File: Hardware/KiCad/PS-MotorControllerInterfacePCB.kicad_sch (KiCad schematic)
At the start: 45 parts, among them J1 53307-2471, J3 PWR + CAN, J4 PEAK, J5 Power MPPT

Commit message: revB
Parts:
- removed J3: PWR + CAN, Connector_Molex:Molex_Nano-Fit_105309-xx06_1x06_P2.50mm_Vertical, symbol Connector_Generic:Conn_01x06
- removed J4: PEAK, Connector_Molex:Molex_Nano-Fit_105309-xx02_1x02_P2.50mm_Vertical, symbol Connector_Generic:Conn_01x02
- removed J5: Power MPPT, UTSVT_Connectors:Molex_Nano-Fit_105309-xx02_1x02_P2.50mm_Vertical, symbol Connector_Generic:Conn_01x02
- removed Moco-in1: MotorController-in, UTSVT_Connectors:Molex_Microfit3.0_02x03_6-Pin-Vertical-PCB-Receptacle_447690601, symbol Connector_Generic:Conn_02x03_Top_Bottom
- removed Moco-out1: MotorController-out, UTSVT_Connectors:Molex_Microfit3.0_02x03_6-Pin-Vertical-PCB-Receptacle_447690601, symbol Connector_Generic:Conn_02x03_Top_Bottom
- removed Z1: SMAF4751A-TP, UTSVT_Passives:SODFL5026X125N, symbol UTSVT_Power:SMAF4749A-TP
- removed Z4: SMAF4744A, UTSVT_Passives:SODFL5026X125N, symbol UTSVT_Power:SMAF4749A-TP
- added 12V?: VIN_24V, TestPoint:TestPoint_Pad_1.0x1.0mm, symbol Connector:TestPoint
- added 12V?: 24V, TestPoint:TestPoint_Pad_1.0x1.0mm, symbol Connector:TestPoint
- added 12V?: 12V, TestPoint:TestPoint_Pad_1.0x1.0mm, symbol Connector:TestPoint
- added 12V?: 12V_BUS, TestPoint:TestPoint_Pad_1.0x1.0mm, symbol Connector:TestPoint
- added D1, D2: D_TVS, symbol Device:D_TVS
- added J2: can out of mppts and moco into board, symbol Connector_Generic:Conn_01x03
- added J3: PWR board, symbol Connector_Generic:Conn_01x02
- added J4: can into board, symbol Connector_Generic:Conn_02x03_Counter_Clockwise
- added J5: can out of board into mppts and moco, symbol Connector_Generic:Conn_01x03
- added J6: Candapter, symbol Connector_Generic:Conn_01x02
- added J8: PWR Moco, symbol Connector_Generic:Conn_01x02
- added J9: can out of board, symbol Connector_Generic:Conn_02x03_Counter_Clockwise
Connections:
- net +12V: now also 12V?.1, J8.1 (Pin_1)
- net +24V: now also 12V?.1, J3.1 (Pin_1)
- net 12V_BUS: now also 12V?.1, D2.2 (A2)
- net CAN_N: now also J2.2 (Pin_2), J4.2 (Pin_2), J5.2 (Pin_2), J6.2 (Pin_2), J9.2 (Pin_2)
- net CAN_P: now also J2.1 (Pin_1), J4.1 (Pin_1), J5.1 (Pin_1), J6.1 (Pin_1), J9.1 (Pin_1)
- net GND: now also D1.1 (A1), D2.1 (A1), J2.3 (Pin_3), J3.2 (Pin_2), J4.3 (Pin_3), J5.3 (Pin_3), J8.2 (Pin_2), J9.3 (Pin_3)
- net VIN_24V: now also 12V?.1, D1.2 (A2)
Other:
- note added: "stub before termination"
- note removed: "VCU -> moco-in -> moco-out -> interface terminate on VCU and interface"
- moved on the sheet: H1, H2, H4, J1, JP1, R11, R12, R17, R_A_TACH_PD1, R_B_TACH_PD1, TP1, TP3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

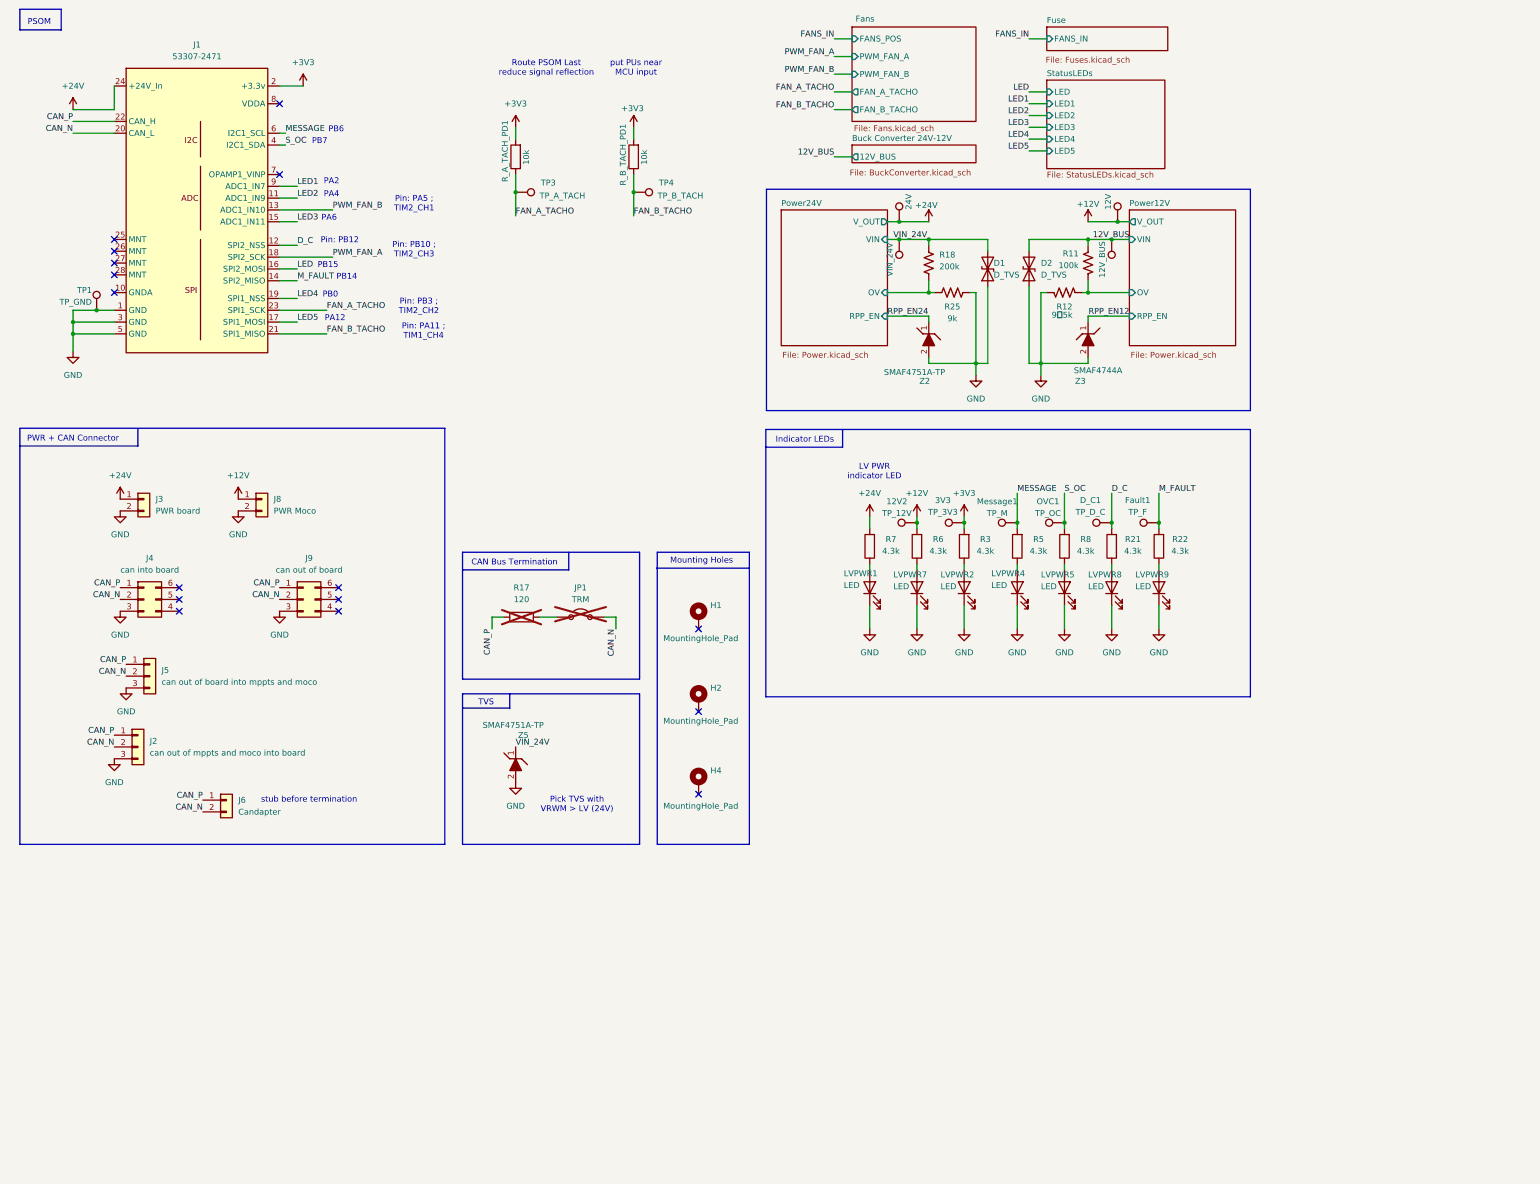
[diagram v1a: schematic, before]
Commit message: schematic changes, pre pcb revB changes
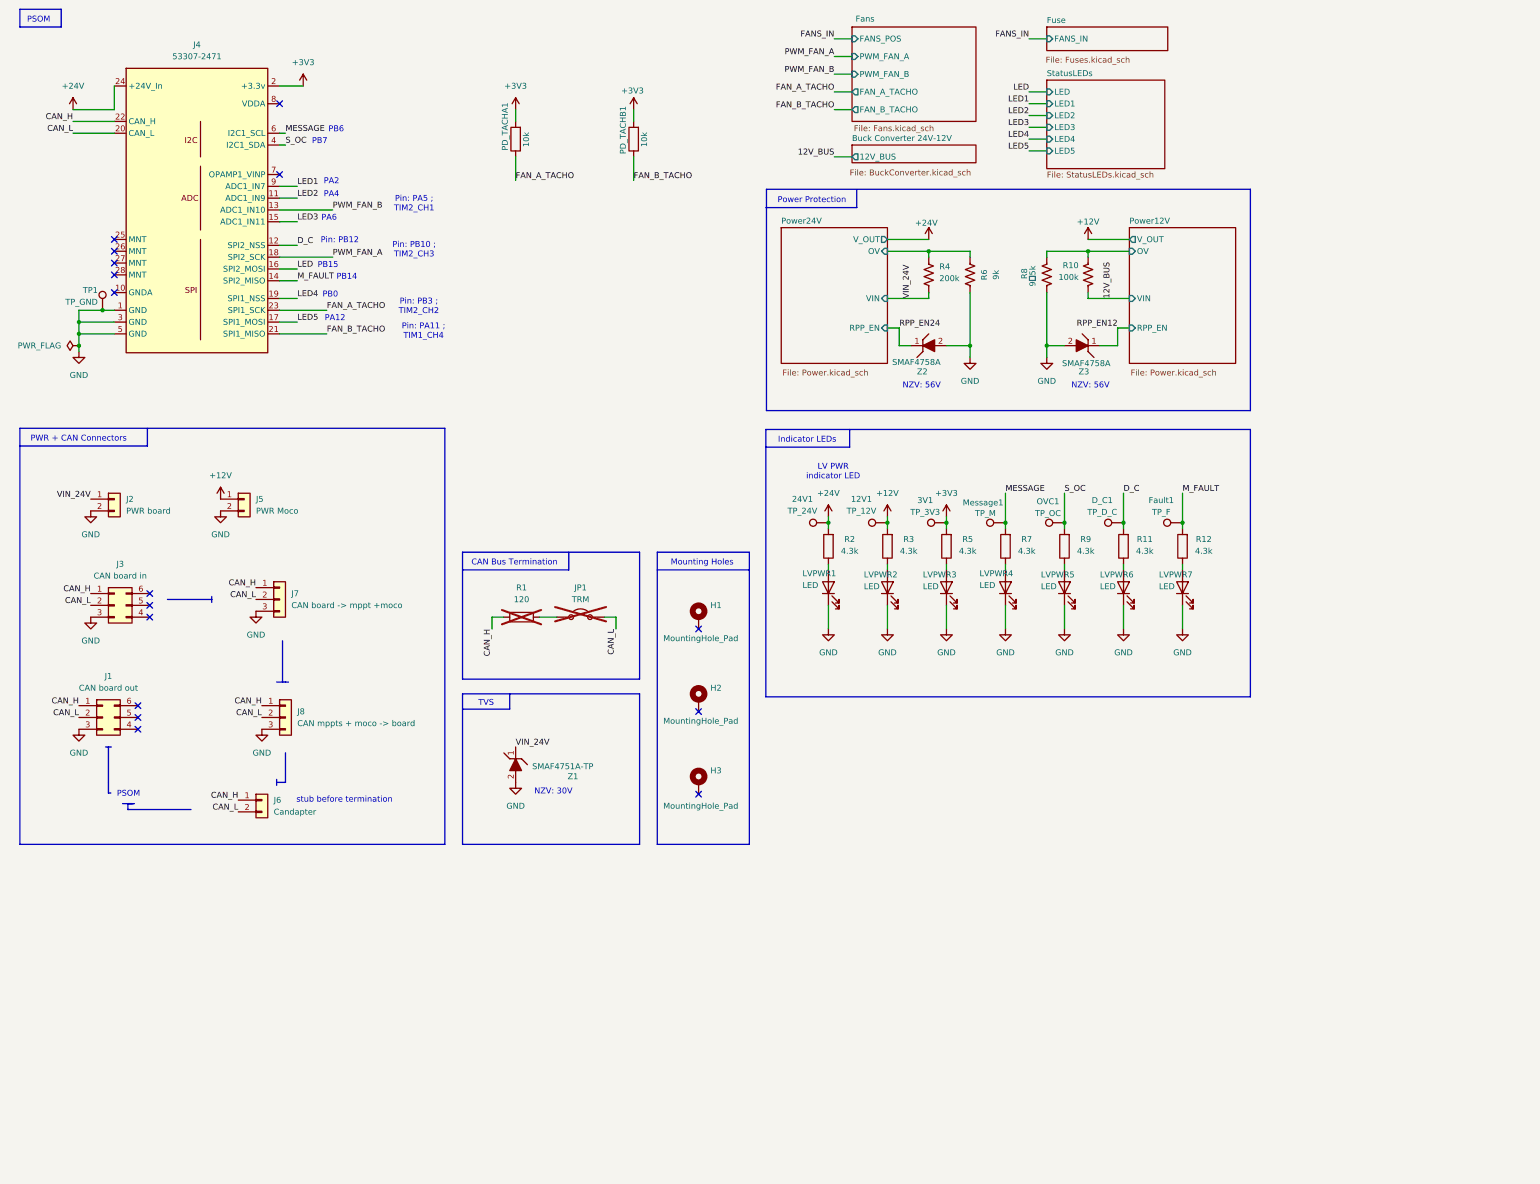
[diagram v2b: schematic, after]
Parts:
- removed 12V?: VIN_24V, TestPoint:TestPoint_Pad_1.0x1.0mm, symbol Connector:TestPoint
- removed 12V?: 24V, TestPoint:TestPoint_Pad_1.0x1.0mm, symbol Connector:TestPoint
- removed 12V?: 12V, TestPoint:TestPoint_Pad_1.0x1.0mm, symbol Connector:TestPoint
- removed 12V?: 12V_BUS, TestPoint:TestPoint_Pad_1.0x1.0mm, symbol Connector:TestPoint
- removed D1, D2: D_TVS, symbol Device:D_TVS
- removed TP3: TP_A_TACH, TestPoint:TestPoint_Pad_1.0x1.0mm, symbol Connector:TestPoint
- removed TP4: TP_B_TACH, TestPoint:TestPoint_Pad_1.0x1.0mm, symbol Connector:TestPoint
- added 24V1: TP_24V, TestPoint:TestPoint_Pad_1.0x1.0mm, symbol Connector:TestPoint
- J1: renamed from J9; value can out of board -> CAN board out; footprint (none) -> Connector_Molex:Molex_Nano-Fit_105314-xx06_2x03_P2.50mm_Horizontal
- J2: renamed from J3; footprint (none) -> Connector_Molex:Molex_Nano-Fit_105313-xx02_1x02_P2.50mm_Horizontal
- J3: renamed from J4; value can into board -> CAN board in; footprint (none) -> Connector_Molex:Molex_Nano-Fit_105314-xx06_2x03_P2.50mm_Horizontal
- J5: renamed from J8; footprint (none) -> Connector_Molex:Molex_Nano-Fit_105313-xx02_1x02_P2.50mm_Horizontal
- J6: footprint (none) -> Connector_Molex:Molex_Nano-Fit_105313-xx02_1x02_P2.50mm_Horizontal
- J7: renamed from J5; value can out of board into mppts and moco -> CAN board -> mppt +moco; footprint (none) -> Connector_Molex:Molex_Nano-Fit_105313-xx03_1x03_P2.50mm_Horizontal
- J8: renamed from J2; value can out of mppts and moco into board -> CAN mppts + moco -> board; footprint (none) -> Connector_Molex:Molex_Nano-Fit_105313-xx03_1x03_P2.50mm_Horizontal
- R1: renamed from R17; LCSC (none) -> C22787
- R10: renamed from R11; LCSC (none) -> C25803
- R11: renamed from R21; LCSC (none) -> C2907165
- R12: renamed from R22; LCSC (none) -> C2907165
- R2: renamed from R7; LCSC (none) -> C2907165
- R3: renamed from R6; LCSC (none) -> C2907165
- R4: renamed from R18; LCSC (none) -> C25811
- R5: renamed from R3; LCSC (none) -> C2907165
- R6: renamed from R25; LCSC (none) -> C166911
- R7: renamed from R5; LCSC (none) -> C2907165
- R9: renamed from R8; LCSC (none) -> C2907165
- Z1: renamed from Z5; LCSC (none) -> C5754725
- Z2: value SMAF4751A-TP -> SMAF4758A; LCSC (none) -> C183490; Mouser Part Number 833-SMAF4751A-TP -> (none)
- Z3: value SMAF4744A -> SMAF4758A; LCSC (none) -> C183490; Mouser Part Number 833-SMAF4744A-TP -> (none)
- renumbered 12V2 to 12V1, 3V3 to 3V1, H4 to H3, J1 to J4, LVPWR7 to LVPWR2, LVPWR2 to LVPWR3, LVPWR8 to LVPWR6, LVPWR9 to LVPWR7, R_A_TACH_PD1 to PD_TACHA1, R_B_TACH_PD1 to PD_TACHB1, R12 to R8
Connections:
- net +24V: now also 24V1.1; no longer J2.1 (Pin_1)
- net 12V_BUS: now also R10.2; no longer R10.1
- net GND: now also R6.1; no longer R6.2
- net Power12V/OV: now also R10.1; no longer R10.2
- net Power24V/OV: now also R4.1, R6.2; no longer R4.2, R6.1
- net VIN_24V: now also J2.1 (Pin_1), R4.2; no longer R4.1
- net CAN_N renamed CAN_L
- net CAN_P renamed CAN_H
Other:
- note added: "NZV: 30V"
- note added: "NZV: 56V"
- note added: "PWR + CAN Connectors"
- note added: "Power Protection"
- note removed: "PWR + CAN Connector"
- note removed: "Pick TVS with VRWM > LV (24V)"
- note removed: "Route PSOM Last reduce signal reflection"
- note removed: "put PUs near MCU input"
- moved on the sheet: 12V1, 3V1, D_C1, Fault1, J1, J2, J3, J5, J6, J7, J8, LVPWR1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

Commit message: sch changes, pre pcb changes
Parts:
- removed PD_TACHA1, PD_TACHB1: 10k, Resistor_SMD:R_0603_1608Metric_Pad0.98x0.95mm_HandSolder, symbol Device:R
- removed R10: 100k, Resistor_SMD:R_0603_1608Metric_Pad0.98x0.95mm_HandSolder, symbol Device:R_US
- removed R4: 200k, Resistor_SMD:R_0603_1608Metric_Pad0.98x0.95mm_HandSolder, symbol Device:R_US
- removed R6: 9k, Resistor_SMD:R_0603_1608Metric_Pad0.98x0.95mm_HandSolder, symbol Device:R_US
- removed R8: 9。5k, Resistor_SMD:R_0603_1608Metric_Pad0.98x0.95mm_HandSolder, symbol Device:R_US
- removed Z2, Z3: SMAF4758A, UTSVT_Passives:SODFL5026X125N, symbol UTSVT_Power:SMAF4749A-TP
- added LED6, LED7: LED, LED_SMD:LED_0603_1608Metric, symbol Device:LED
- added R7, R8: 4.3k, Resistor_SMD:R_0603_1608Metric_Pad0.98x0.95mm_HandSolder, symbol Device:R
- added TP_1: LED1, TestPoint:TestPoint_Pad_1.0x1.0mm, symbol Connector:TestPoint
- added TP_2: LED2, TestPoint:TestPoint_Pad_1.0x1.0mm, symbol Connector:TestPoint
- D_C1: value TP_D_C -> TP_DC
- H1, H2, H3: footprint MountingHole:MountingHole_3.2mm_M3 -> MountingHole:MountingHole_3.2mm_M3_Pad_TopBottom
- J1: renamed from J2; footprint Connector_Molex:Molex_Nano-Fit_105313-xx02_1x02_P2.50mm_Horizontal -> UTSVT_Connectors:105313-2102
- J2: renamed from J1; footprint Connector_Molex:Molex_Nano-Fit_105314-xx06_2x03_P2.50mm_Horizontal -> UTSVT_Connectors:105314-1306
- J3: footprint Connector_Molex:Molex_Nano-Fit_105314-xx06_2x03_P2.50mm_Horizontal -> UTSVT_Connectors:105314-1306
- J4: renamed from J6; footprint Connector_Molex:Molex_Nano-Fit_105313-xx02_1x02_P2.50mm_Horizontal -> UTSVT_Connectors:105313-2102
- J6: renamed from J7; footprint Connector_Molex:Molex_Nano-Fit_105313-xx03_1x03_P2.50mm_Horizontal -> UTSVT_Connectors:105313-1103
- J7: renamed from J8; footprint Connector_Molex:Molex_Nano-Fit_105313-xx03_1x03_P2.50mm_Horizontal -> UTSVT_Connectors:105313-1103
- J8: renamed from J5; footprint Connector_Molex:Molex_Nano-Fit_105313-xx02_1x02_P2.50mm_Horizontal -> UTSVT_Connectors:105313-2102
- renumbered J4 to J5, LVPWR3 to LED1, LVPWR4 to LED2, LVPWR5 to LED3, LVPWR6 to LED4, LVPWR7 to LED5, LVPWR2 to LED8, R5 to R1, R3 to R10, R7 to R2, R9 to R3, R1 to R4, R11 to R5, R12 to R6, R2 to R9
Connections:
- net LED4 is gone; now on net LED1: J5.19 (SPI1_NSS)
- net LED5 is gone; now on net LED2: J5.17 (SPI1_MOSI)
- net VIN_24V is gone; now on net +24V: J1.1 (Pin_1), Z1.1 (K)
- net +24V: no longer 24V1.1, R9.2
- net GND: now also LED6.1 (K), LED7.1 (K)
- net LED1: now also R7.2, TP_1.1; no longer J5.9 (ADC1_IN7)
- net LED2: now also R8.2, TP_2.1; no longer J5.11 (ADC1_IN9)
- net LED renamed LATCH
- net LED3 renamed ST
- new net: LED6.2 (A), R7.1
- new net: LED7.2 (A), R8.1
- new net 12V_SENSE: J5.9 (ADC1_IN7)
- new net Buck Converter 24V-12V/24VIN: 24V1.1, R9.2
- new net EN: J5.11 (ADC1_IN9)
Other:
- removed sheet Fuse
- removed sheet Power24V
- removed sheet StatusLEDs
- added sheet HSS (HSS.kicad_sch)
- sheet Buck Converter 24V-12V ports: added 12V_SENSE, 24VIN; removed none
- sheet Power12V ports: added VOUT; removed OV, RPP_EN, V_OUT
- note added: "CAN Connectors"
- note removed: "Indicator LEDs"
- note removed: "LV PWR indicator LED"
- note removed: "NZV: 56V"
- note removed: "PWR + CAN Connectors"
- note removed: "Power Protection"
- note removed: "TVS"
- moved on the sheet: 12V1, 24V1, 3V1, D_C1, Fault1, H1, H2, H3, J1, J2, J3, J4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

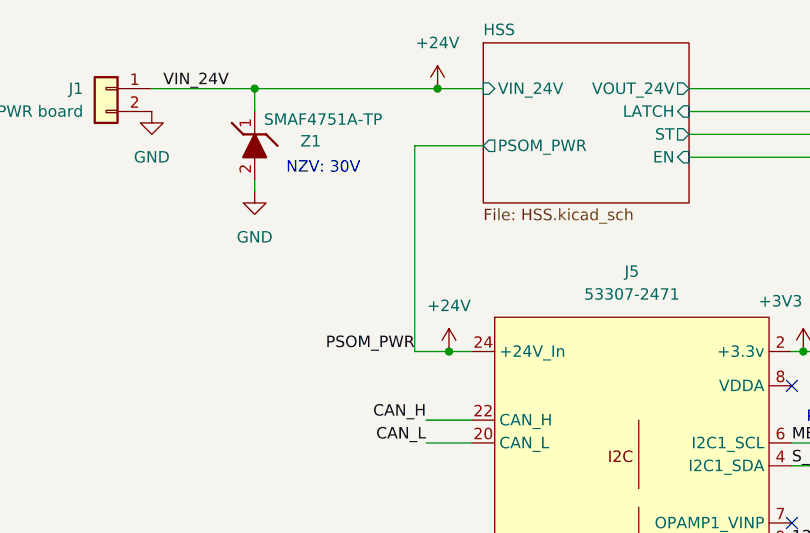
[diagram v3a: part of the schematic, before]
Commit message: fuse fix
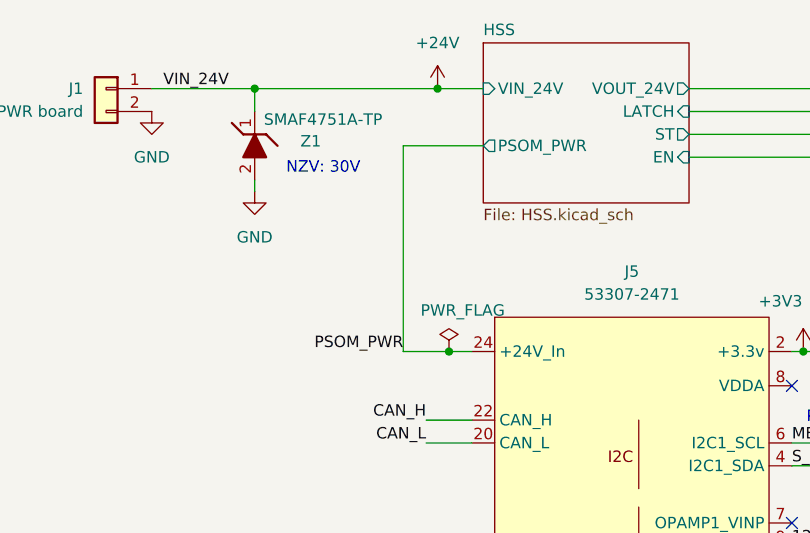
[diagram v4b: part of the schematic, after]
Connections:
- net +24V: no longer J5.24 (+24V_In)
- new net PSOM_PWR: J5.24 (+24V_In)
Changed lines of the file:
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@@
 	)
 	(junction
-		(at 77.47 62.23)
-		(diameter 0)
-		(color 0 0 0 0)
-	)
-	(junction
 		(at 72.39 118.11)
 		(diameter 0)
@@
 	)
 	(junction
+		(at 77.47 62.23)
+		(diameter 0)
+		(color 0 0 0 0)
+	)
+	(junction
 		(at 116.84 62.23)
 		(diameter 0)
@@
 	(wire
 		(pts
+			(xy 72.39 62.23) (xy 77.47 62.23)
+		)
+		(stroke
+			(width 0)
+			(type default)
+		)
+	)
+	(wire
+		(pts
 			(xy 163.83 40.64) (xy 104.14 40.64)
 		)
@@
 	(wire
 		(pts
-			(xy 73.66 39.37) (xy 81.28 39.37)
+			(xy 72.39 39.37) (xy 81.28 39.37)
 		)
 		(stroke
@@
 		)
 	)
-	(wire
-		(pts
-			(xy 73.66 62.23) (xy 77.47 62.23)
-		)
-		(stroke
-			(width 0)
-			(type default)
-		)
-	)
 	(polyline
 		(pts
@@
 	(wire
 		(pts
-			(xy 77.47 62.23) (xy 80.01 62.23)
+			(xy 166.37 38.1) (xy 166.37 91.44)
 		)
 		(stroke
@@
 	(wire
 		(pts
-			(xy 166.37 38.1) (xy 166.37 91.44)
+			(xy 77.47 62.23) (xy 80.01 62.23)
 		)
 		(stroke
@@
 	(wire
 		(pts
-			(xy 73.66 62.23) (xy 73.66 39.37)
+			(xy 72.39 62.23) (xy 72.39 39.37)
 		)
 		(stroke
@@
 	)
 	(label "PSOM_PWR"
-		(at 73.66 62.23 180)
+		(at 72.39 62.23 180)
 		(effects
 			(font
@@
 	)
 	(symbol
-		(lib_id "power:+24V")
-		(at 77.47 62.23 0)
-		(unit 1)
-		(exclude_from_sim no)
-		(in_bom yes)
-		(on_board yes)
-		(dnp no)
-		(fields_autoplaced yes)
-		(property "Reference" "#PWR07"
-			(at 77.47 66.04 0)
-			(effects
-				(font
-					(size 1.27 1.27)
-				)
-				(hide yes)
-			)
-		)
-		(property "Value" "+24V"
-			(at 77.47 57.15 0)
-			(effects
-				(font
-					(size 1.27 1.27)
-				)
-			)
-		)
-		(property "Footprint" ""
-			(at 77.47 62.23 0)
-			(effects
-				(font
-					(size 1.27 1.27)
-				)
-				(hide yes)
-			)
-		)
-		(property "Datasheet" ""
-			(at 77.47 62.23 0)
-			(effects
-				(font
-					(size 1.27 1.27)
-				)
-				(hide yes)
-			)
-		)
-		(property "Description" "Power symbol creates a global label with name \"+24V\""
-			(at 77.47 62.23 0)
-			(effects
-				(font
-					(size 1.27 1.27)
-				)
-				(hide yes)
-			)
-		)
-		(pin "1"
-		)
-		(instances
-			(project "PS-MotorControllerInterfacePCB"
-				(path "/a2e13c19-ff3a-4e43-a7f5-200fd5b2b978"
-					(reference "#PWR07")
-					(unit 1)
-				)
-			)
-		)
-	)
-	(symbol
 		(lib_id "power:GND")
 		(at 153.67 76.2 0)
@@
 					(unit 1)
 				)
+			)
+		)
+	)
+	(symbol
+		(lib_id "power:PWR_FLAG")
+		(at 77.47 62.23 0)
+		(unit 1)
+		(exclude_from_sim no)
+		(in_bom yes)
+		(on_board yes)
+		(dnp no)
+		(property "Reference" "#FLG04"
+			(at 77.47 60.325 0)
+			(effects
+				(font
+					(size 1.27 1.27)
+				)
+				(hide yes)
+			)
+		)
+		(property "Value" "PWR_FLAG"
+			(at 78.994 57.658 0)
+			(effects
+				(font
+					(size 1.27 1.27)
+				)
+			)
+		)
+		(property "Footprint" ""
+			(at 77.47 62.23 0)
+			(effects
+				(font
+					(size 1.27 1.27)
+				)
+				(hide yes)
+			)
+		)
+		(property "Datasheet" "~"
+			(at 77.47 62.23 0)
+			(effects
+				(font
+					(size 1.27 1.27)
+				)
+				(hide yes)
+			)
+		)
+		(property "Description" "Special symbol for telling ERC where power comes from"
+			(at 77.47 62.23 0)
+			(effects
+				(font
+					(size 1.27 1.27)
+				)
+				(hide yes)
+			)
+		)
+		(pin "1"
+		)
+		(instances
+			(project ""
+				(path "/a2e13c19-ff3a-4e43-a7f5-200fd5b2b978"
+					(reference "#FLG04")
+					(unit 1)
+				)
